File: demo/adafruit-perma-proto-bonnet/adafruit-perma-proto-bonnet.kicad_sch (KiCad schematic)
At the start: 2 parts

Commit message: Add corner mounting holes on perma proto board
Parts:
- added H1, H2, H3, H4: MountingHole, MountingHole:MountingHole_2.7mm_M2.5, symbol Mechanical:MountingHole

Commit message: Add test 1206 LED and Resistor in bonnet PCB
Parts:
- added D1: IR26-21C_L110_TR8, LED_SMD:LED_1206_3216Metric, symbol LED:IR26-21C_L110_TR8
- added R1: R, Resistor_SMD:R_1206_3216Metric, symbol Device:R
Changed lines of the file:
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@@
+	)
+	(symbol
+		(lib_id "Device:R")
+		(at 76.2 161.29 0)
+		(unit 1)
+		(exclude_from_sim no)
+		(in_bom yes)
+		(on_board yes)
+		(dnp no)
+		(fields_autoplaced yes)
+		(property "Reference" "R1"
+			(at 78.74 160.0199 0)
+			(effects
+				(font
+					(size 1.27 1.27)
+				)
+				(justify left)
+			)
+		)
+		(property "Value" "R"
+			(at 78.74 162.5599 0)
+			(effects
+				(font
+					(size 1.27 1.27)
+				)
+				(justify left)
+			)
+		)
+		(property "Footprint" "Resistor_SMD:R_1206_3216Metric"
+			(at 74.422 161.29 90)
+			(effects
+				(font
+					(size 1.27 1.27)
+				)
+				(hide yes)
+			)
+		)
+		(property "Datasheet" "~"
+			(at 76.2 161.29 0)
+			(effects
+				(font
+					(size 1.27 1.27)
+				)
+				(hide yes)
+			)
+		)
+		(property "Description" "Resistor"
+			(at 76.2 161.29 0)
+			(effects
+				(font
+					(size 1.27 1.27)
+				)
+				(hide yes)
+			)
+		)
+		(pin "1"
+		)
+		(pin "2"
+		)
+		(instances
+			(project ""
+				(path "/41d93e62-51cf-4ee0-9812-46e0e0ff0b6b"
+					(reference "R1")
+					(unit 1)
+				)
+			)
+		)
+	)
+	(symbol
+		(lib_id "LED:IR26-21C_L110_TR8")
+		(at 62.23 162.56 0)
+		(unit 1)
+		(exclude_from_sim no)
+		(in_bom yes)
+		(on_board yes)
+		(dnp no)
+		(fields_autoplaced yes)
+		(property "Reference" "D1"
+			(at 60.6425 156.21 0)
+			(effects
+				(font
+					(size 1.27 1.27)
+				)
+			)
+		)
+		(property "Value" "IR26-21C_L110_TR8"
+			(at 60.6425 158.75 0)
+			(effects
+				(font
+					(size 1.27 1.27)
+				)
+			)
+		)
+		(property "Footprint" "LED_SMD:LED_1206_3216Metric"
+			(at 62.23 157.48 0)
+			(effects
+				(font
+					(size 1.27 1.27)
+				)
+				(hide yes)
+			)
+		)
+		(property "Datasheet" "http://www.everlight.com/file/ProductFile/IR26-21C-L110-TR8.pdf"
+			(at 62.23 162.56 0)
+			(effects
+				(font
+					(size 1.27 1.27)
+				)
+				(hide yes)
+			)
+		)
+		(property "Description" "940nm, 20 deg, Infrared LED, 1206"
+			(at 62.23 162.56 0)
+			(effects
+				(font
+					(size 1.27 1.27)
+				)
+				(hide yes)
+			)
+		)
+		(pin "2"
+		)
+		(pin "1"
+		)
+		(instances
+			(project ""
+				(path "/41d93e62-51cf-4ee0-9812-46e0e0ff0b6b"
+					(reference "D1")
+					(unit 1)
+				)
+			)
+		)
 	)
 	(symbol

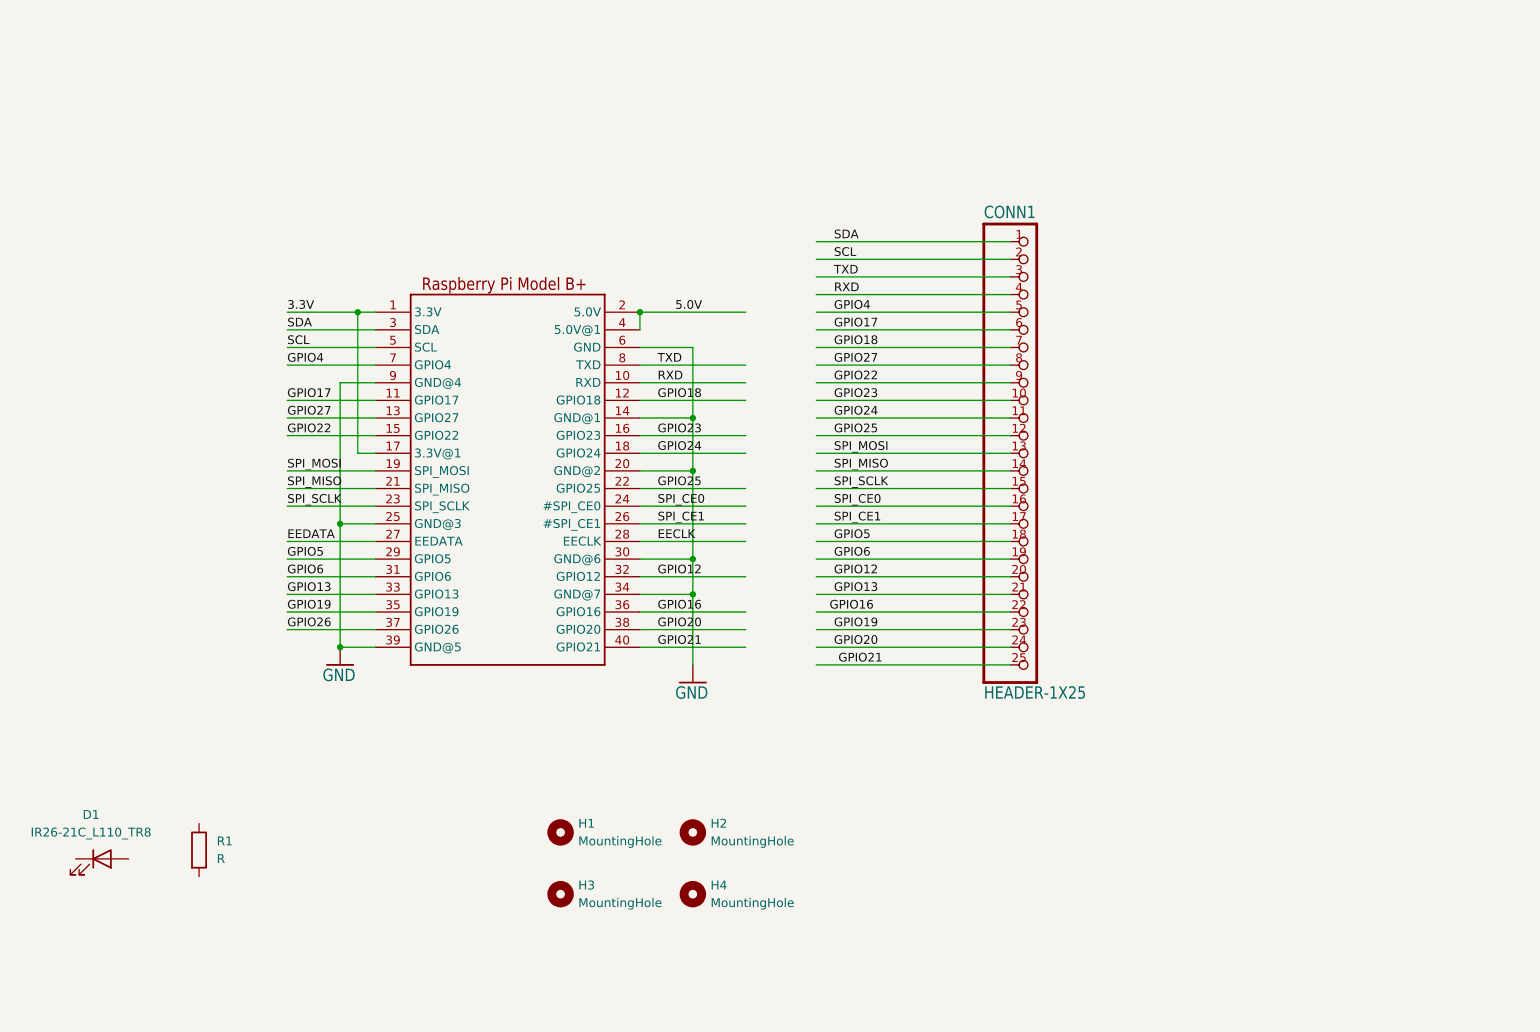
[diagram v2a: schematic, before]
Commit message: Populate demo board with 9 LEDs
Location moved to lower row. Resistors are placed such that they
connect to ground. Shell gap increased slightly so that LED can
sit comfortably - probably will be loose for the resistor. Can
be tuned further.
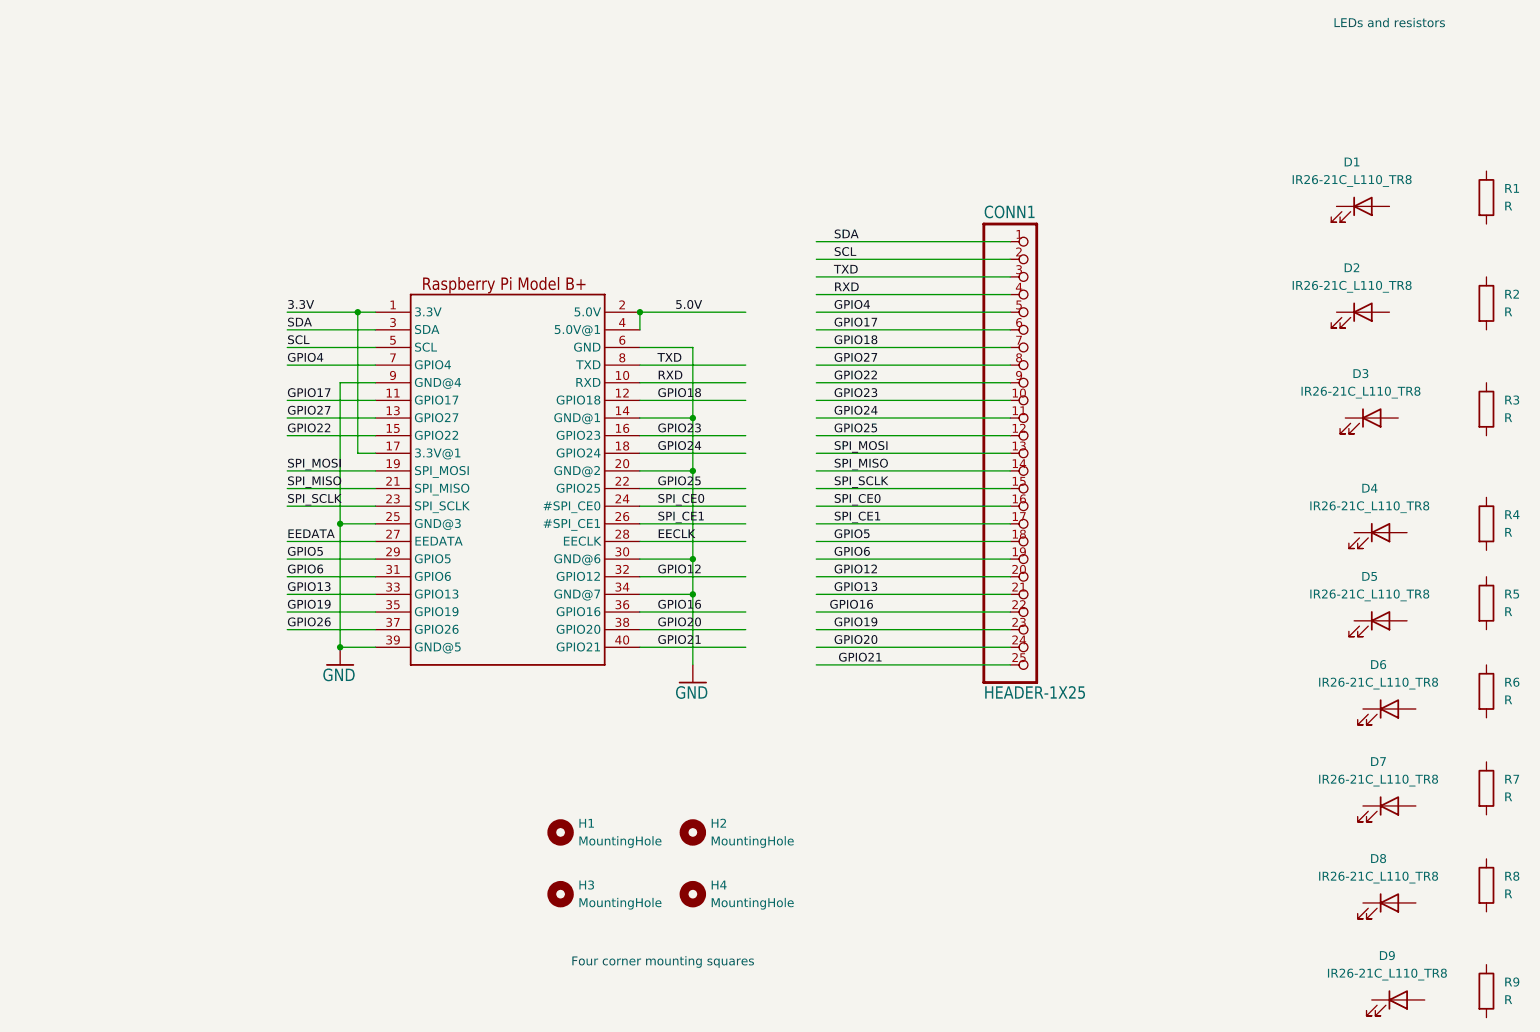
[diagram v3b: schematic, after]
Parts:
- added D2, D3, D4, D5, D6, D7, D8, D9: IR26-21C_L110_TR8, LED_SMD:LED_1206_3216Metric, symbol LED:IR26-21C_L110_TR8
- added R2, R3, R4, R5, R6, R7, R8, R9: R, Resistor_SMD:R_1206_3216Metric, symbol Device:R
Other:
- note added: "Four corner mounting squares"
- note added: "LEDs and resistors"
- moved on the sheet: D1, R1
